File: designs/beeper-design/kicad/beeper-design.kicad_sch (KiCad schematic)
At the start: 0 parts

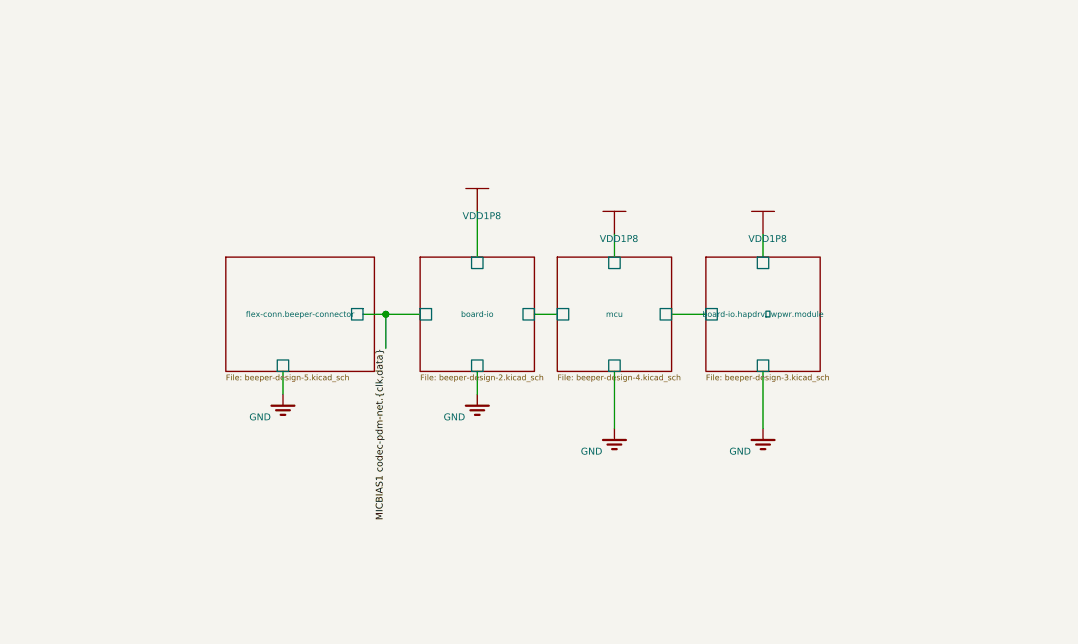
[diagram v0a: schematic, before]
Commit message: made ocdb a submodule
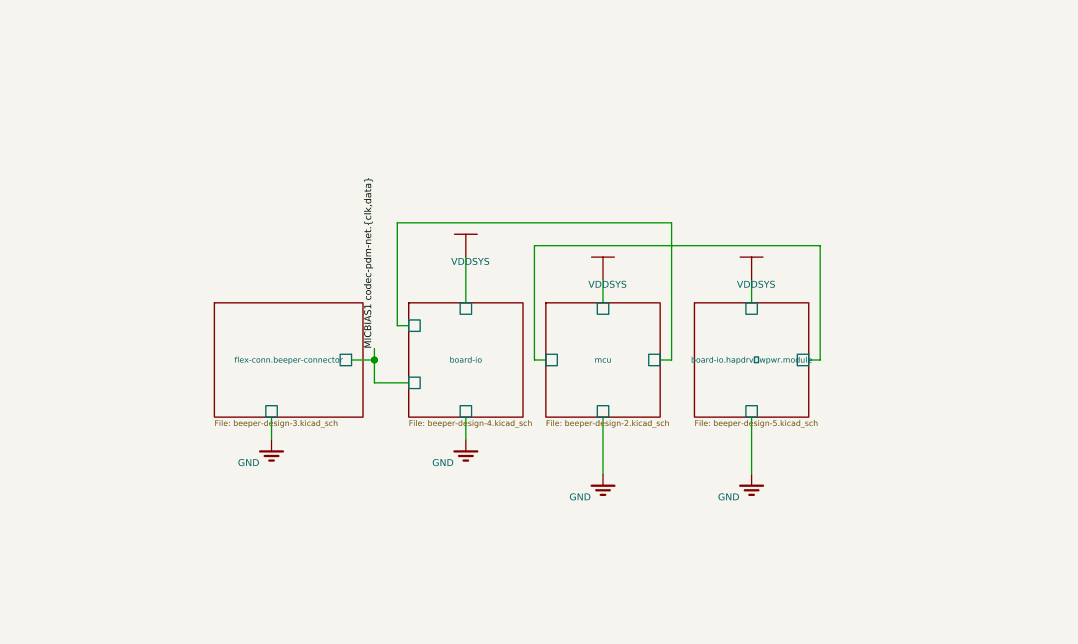
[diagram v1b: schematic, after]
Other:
- sheet board-io: file beeper-design-2.kicad_sch -> beeper-design-4.kicad_sch
- sheet board-io.hapdrv wpwr.module: file beeper-design-3.kicad_sch -> beeper-design-5.kicad_sch
- sheet flex-conn.beeper-connector: file beeper-design-5.kicad_sch -> beeper-design-3.kicad_sch
- sheet mcu: file beeper-design-4.kicad_sch -> beeper-design-2.kicad_sch

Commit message: kicad exported data
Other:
- sheet board-io: file beeper-design-4.kicad_sch -> beeper-design-2.kicad_sch
- sheet board-io.hapdrv wpwr.module: file beeper-design-5.kicad_sch -> beeper-design-3.kicad_sch
- sheet flex-conn.beeper-connector: file beeper-design-3.kicad_sch -> beeper-design-5.kicad_sch
- sheet mcu: file beeper-design-2.kicad_sch -> beeper-design-4.kicad_sch

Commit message: another export
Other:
- removed sheet board-io.hapdrv wpwr.module
- removed sheet flex-conn.beeper-connector
- added sheet board-io.hapdrv (beeper-design-2.kicad_sch)
- added sheet flex-conn.beeper-connector wpwr.module (beeper-design-3.kicad_sch)
- added sheet mcu.mem.module (beeper-design-5.kicad_sch)
- sheet board-io: file beeper-design-2.kicad_sch -> beeper-design-6.kicad_sch

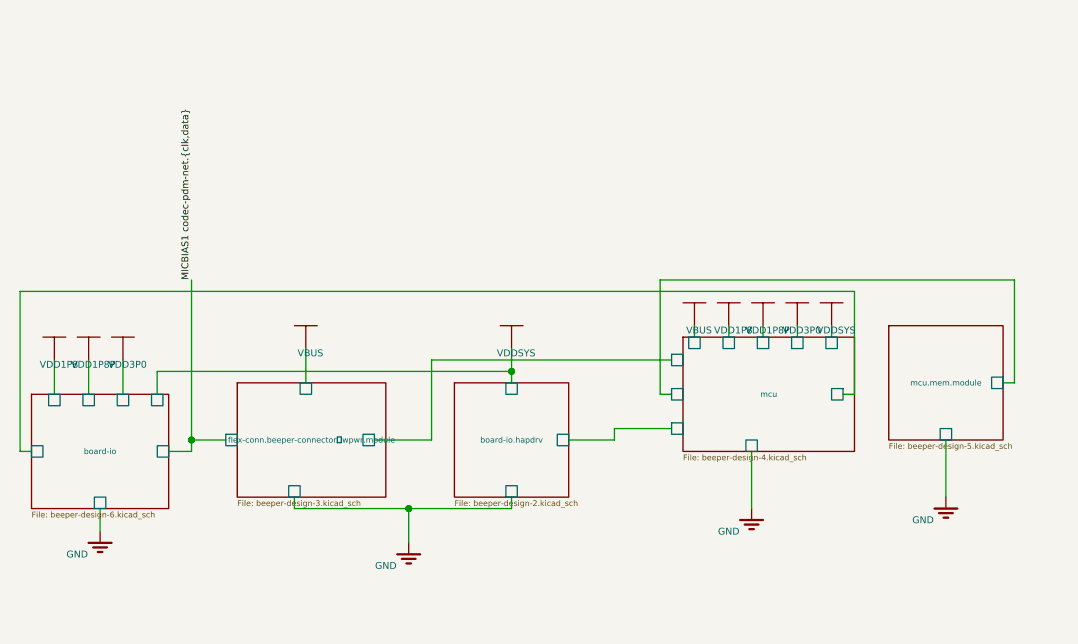
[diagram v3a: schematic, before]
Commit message: crash with new usb connector
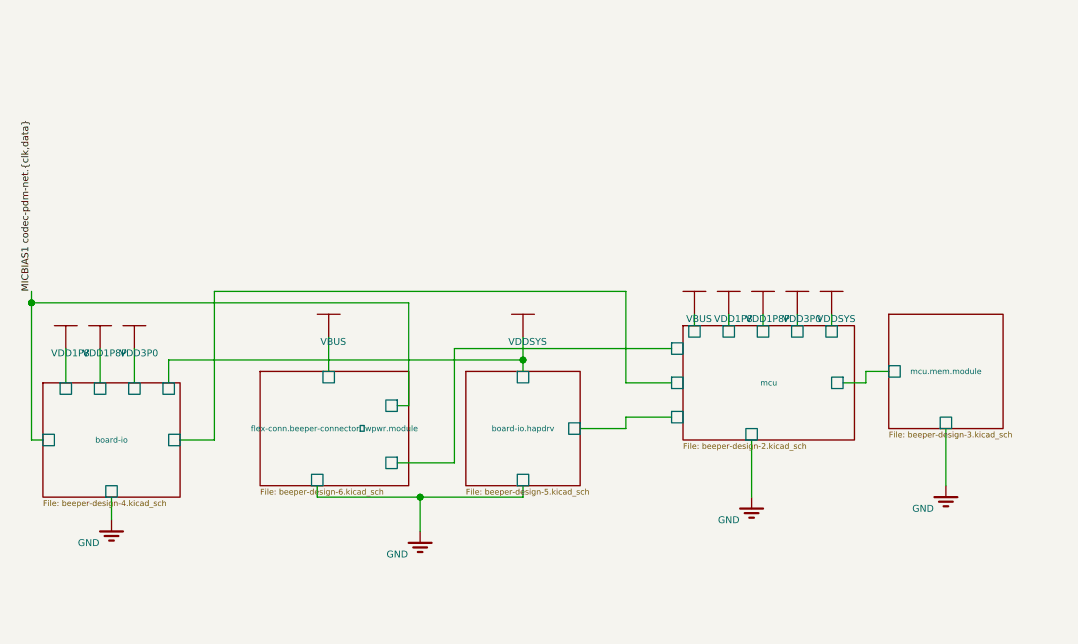
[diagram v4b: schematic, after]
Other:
- sheet board-io: file beeper-design-6.kicad_sch -> beeper-design-4.kicad_sch
- sheet board-io.hapdrv: file beeper-design-2.kicad_sch -> beeper-design-5.kicad_sch
- sheet flex-conn.beeper-connector wpwr.module: file beeper-design-3.kicad_sch -> beeper-design-6.kicad_sch
- sheet mcu: file beeper-design-4.kicad_sch -> beeper-design-2.kicad_sch
- sheet mcu.mem.module: file beeper-design-5.kicad_sch -> beeper-design-3.kicad_sch

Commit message: new export
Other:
- sheet board-io: file beeper-design-4.kicad_sch -> beeper-design-2.kicad_sch
- sheet board-io.hapdrv: file beeper-design-5.kicad_sch -> beeper-design-3.kicad_sch
- sheet flex-conn.beeper-connector wpwr.module: file beeper-design-6.kicad_sch -> beeper-design-4.kicad_sch
- sheet mcu: file beeper-design-2.kicad_sch -> beeper-design-5.kicad_sch
- sheet mcu.mem.module: file beeper-design-3.kicad_sch -> beeper-design-6.kicad_sch

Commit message: reasonble export
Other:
- sheet board-io: file beeper-design-2.kicad_sch -> beeper-design-3.kicad_sch
- sheet board-io.hapdrv: file beeper-design-3.kicad_sch -> beeper-design-4.kicad_sch
- sheet flex-conn.beeper-connector wpwr.module: file beeper-design-4.kicad_sch -> beeper-design-5.kicad_sch
- sheet mcu: file beeper-design-5.kicad_sch -> beeper-design-6.kicad_sch
- sheet mcu.mem.module: file beeper-design-6.kicad_sch -> beeper-design-2.kicad_sch

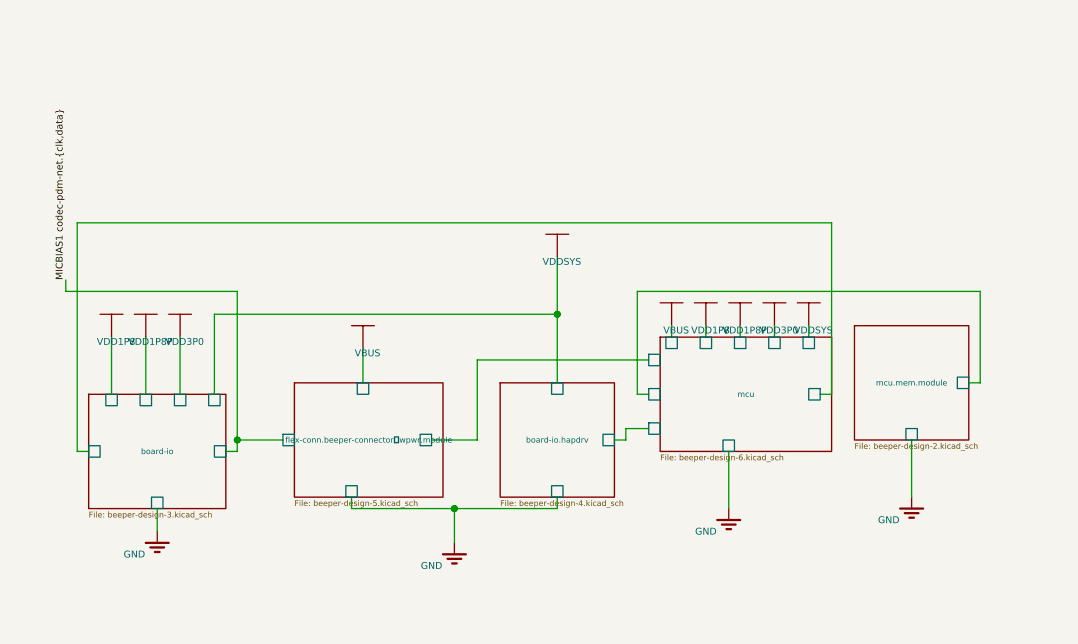
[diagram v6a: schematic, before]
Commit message: exported, yet XTALM32p keeps disappearing
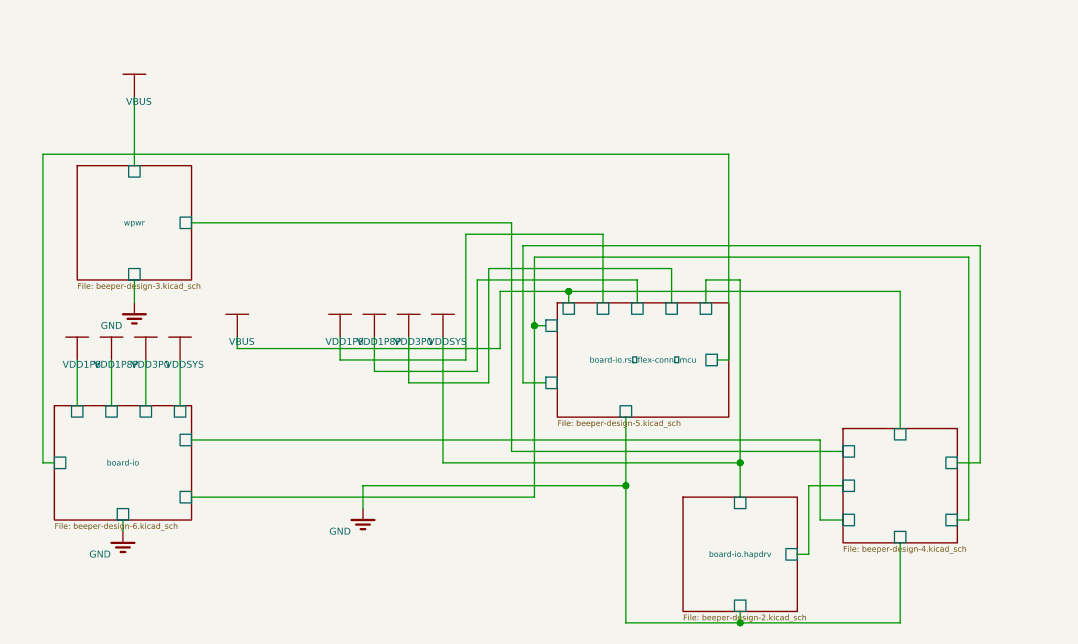
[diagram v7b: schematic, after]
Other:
- removed sheet flex-conn.beeper-connector wpwr.module
- removed sheet mcu
- removed sheet mcu.mem.module
- added sheet  (beeper-design-4.kicad_sch)
- added sheet board-io.rs flex-conn mcu (beeper-design-5.kicad_sch)
- added sheet wpwr (beeper-design-3.kicad_sch)
- sheet board-io: file beeper-design-3.kicad_sch -> beeper-design-6.kicad_sch
- sheet board-io.hapdrv: file beeper-design-4.kicad_sch -> beeper-design-2.kicad_sch

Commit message: fixed up pours, keepout regions
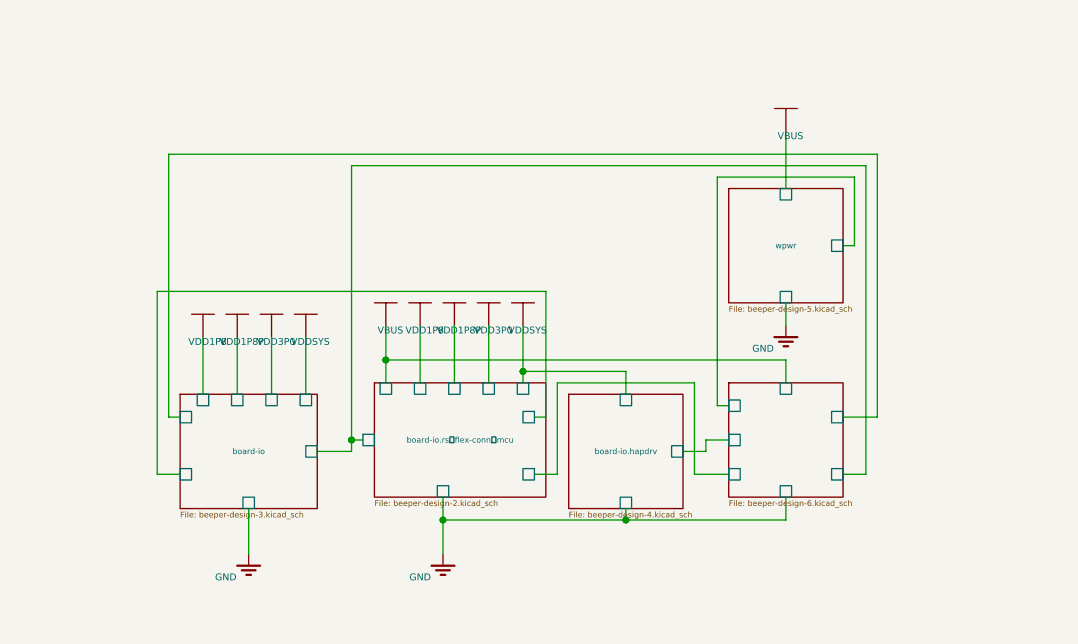
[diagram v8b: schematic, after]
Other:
- sheet : file beeper-design-4.kicad_sch -> beeper-design-6.kicad_sch
- sheet board-io: file beeper-design-6.kicad_sch -> beeper-design-3.kicad_sch
- sheet board-io.hapdrv: file beeper-design-2.kicad_sch -> beeper-design-4.kicad_sch
- sheet board-io.rs flex-conn mcu: file beeper-design-5.kicad_sch -> beeper-design-2.kicad_sch
- sheet wpwr: file beeper-design-3.kicad_sch -> beeper-design-5.kicad_sch
